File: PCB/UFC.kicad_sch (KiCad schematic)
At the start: 56 parts, among them M1 Fan_3pin, M2 Fan_3pin, M3 Fan_3pin, M4 Fan_3pin, M5 Fan_3pin, M6 Fan_3pin, M7 Fan_3pin, M8 Fan_3pin, SW1 PWM 12:5, U1 Pico

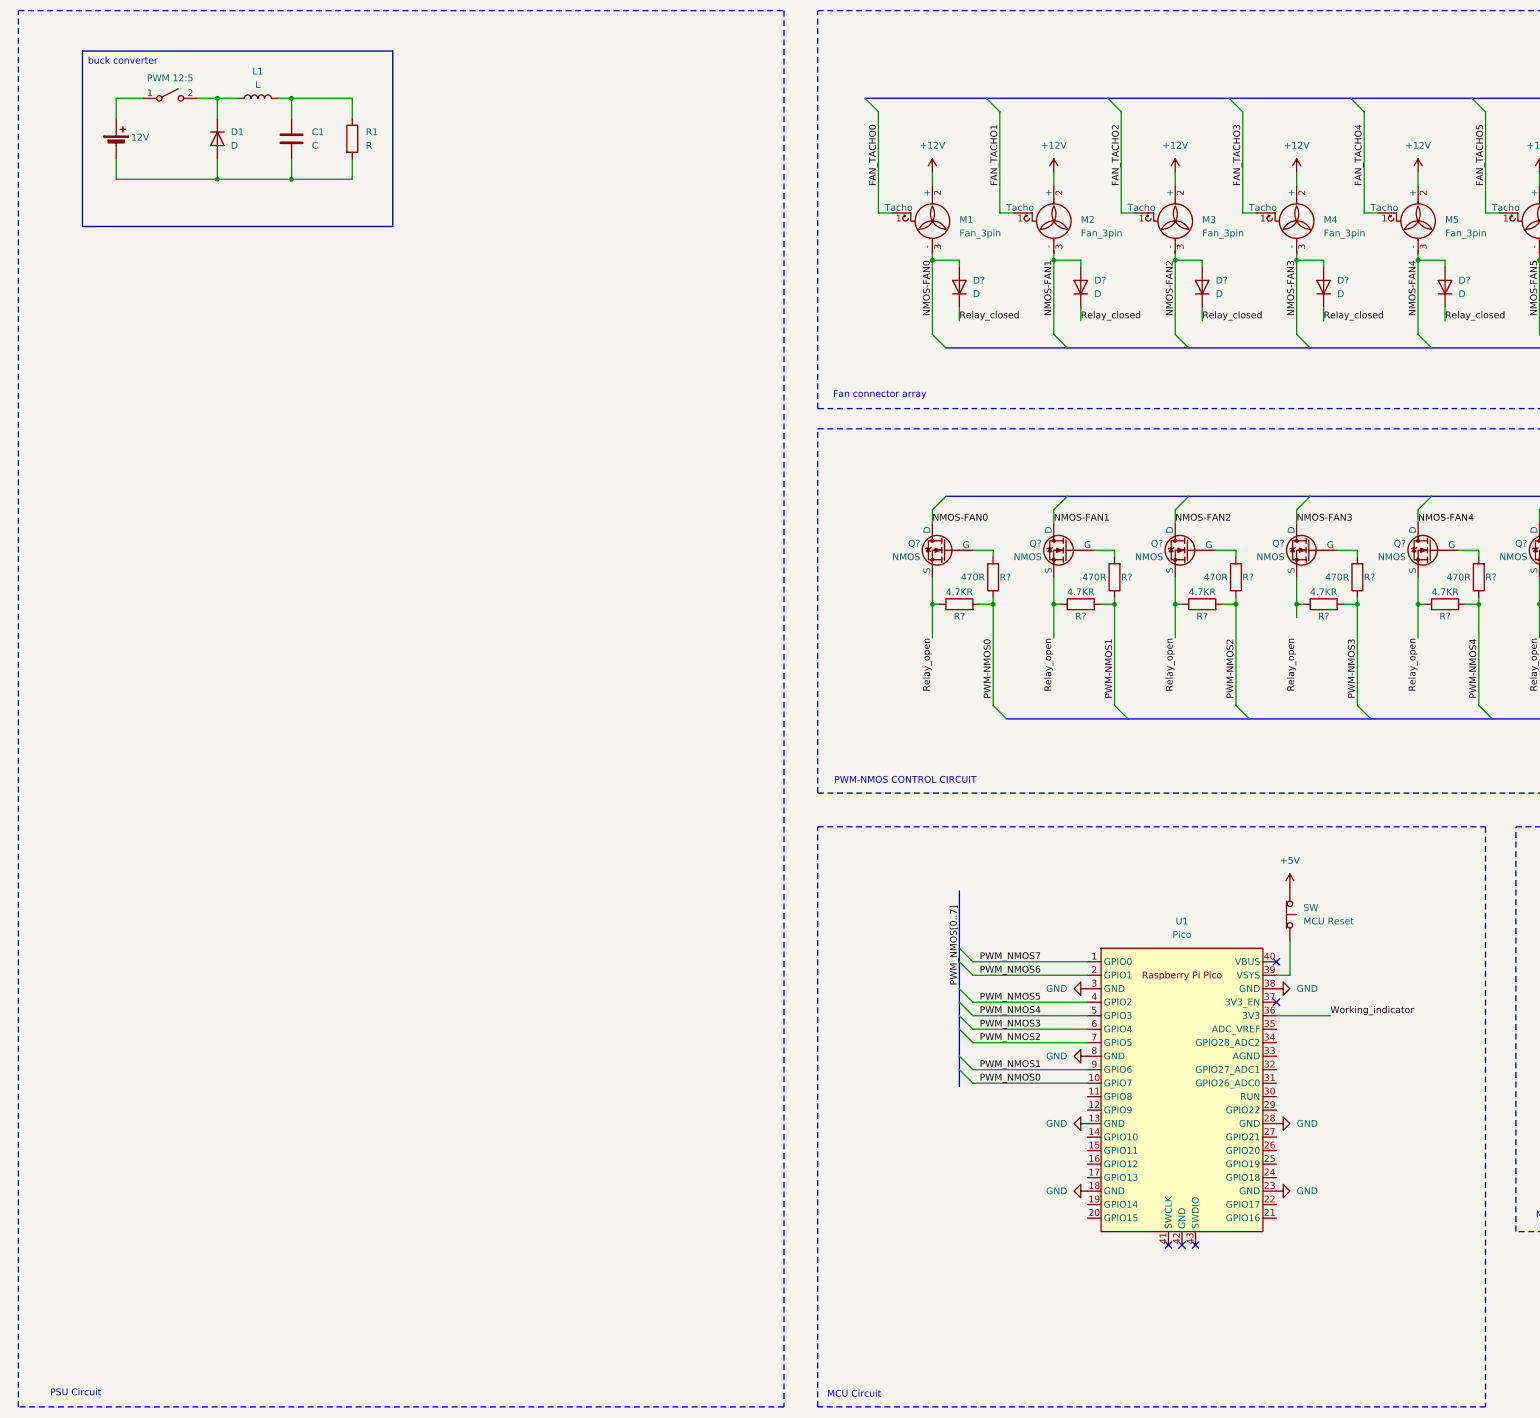
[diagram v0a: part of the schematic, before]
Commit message: Scheme circuit placement change
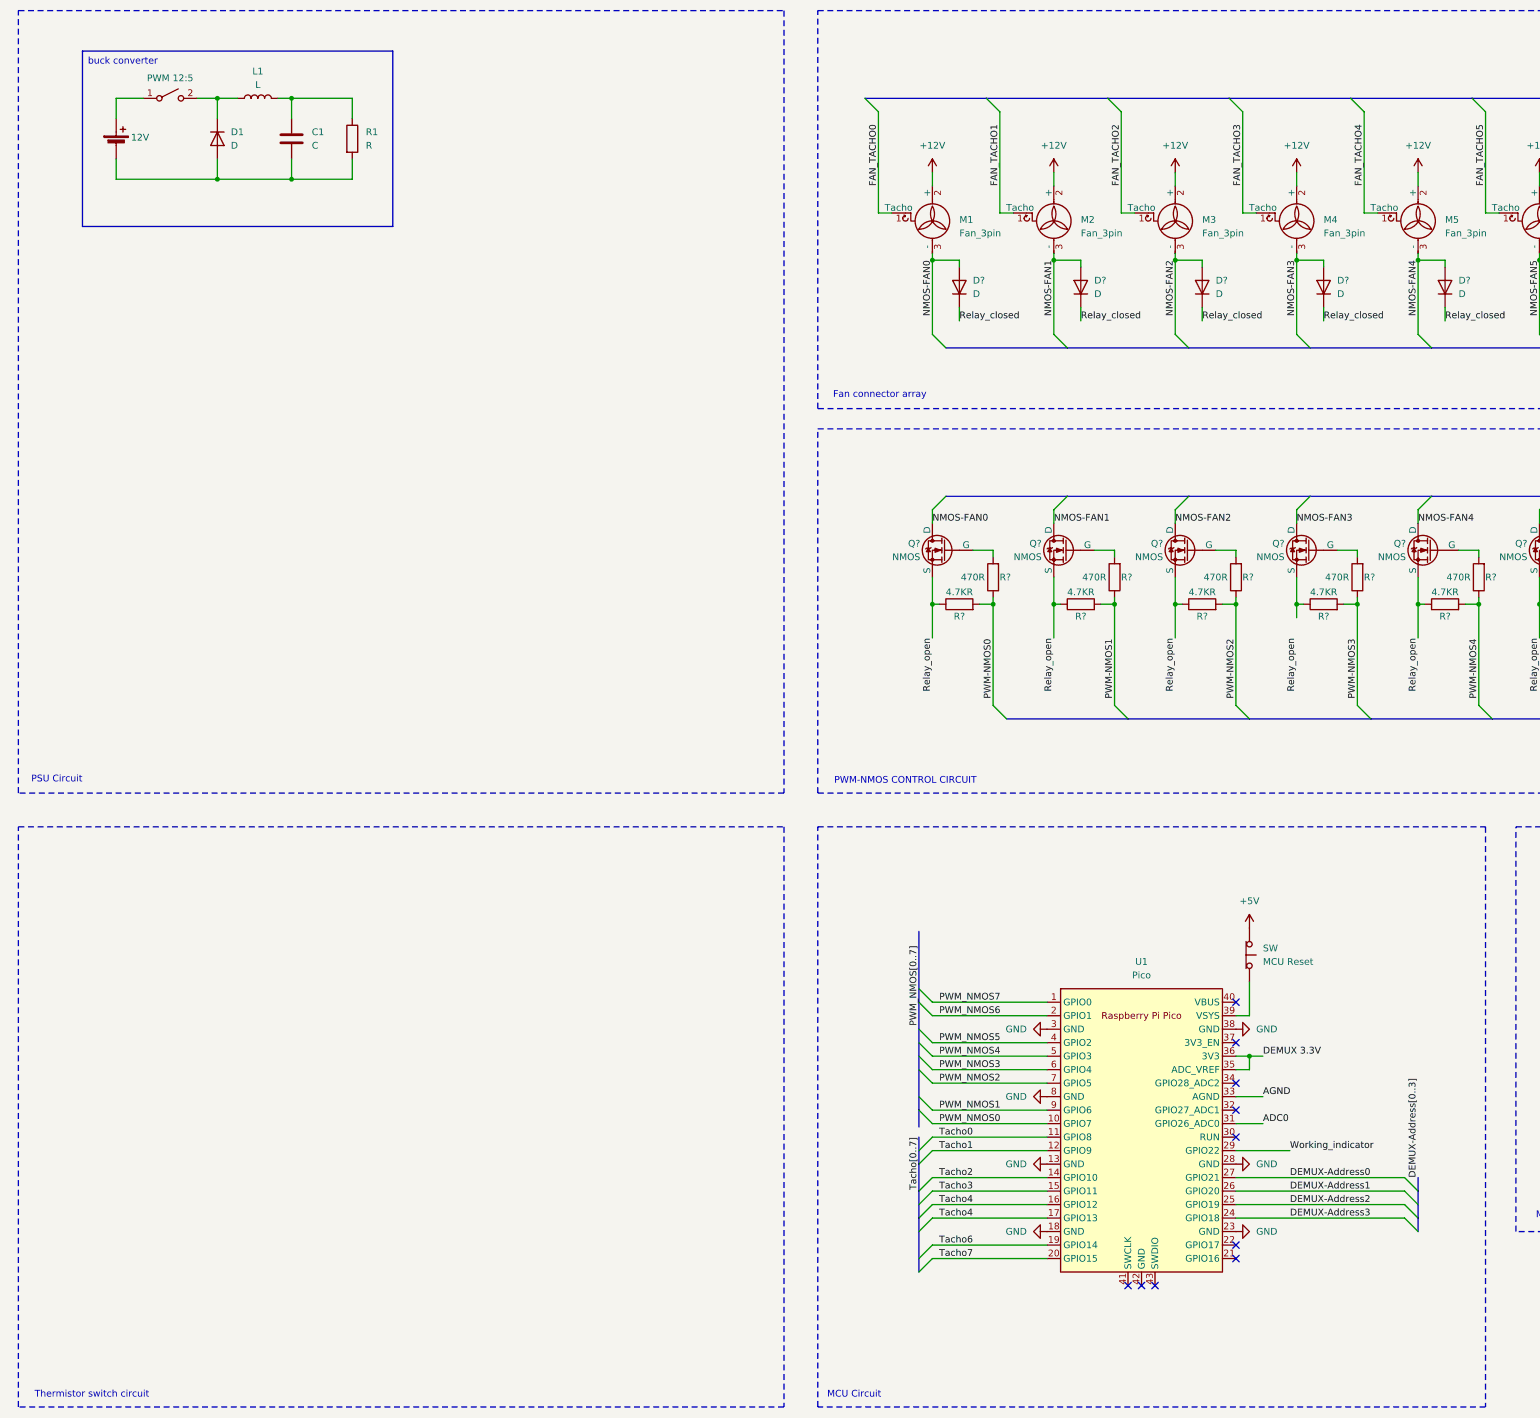
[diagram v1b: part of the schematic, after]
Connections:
- net Working_indicator: now also U1.29 (GPIO22); no longer U1.36 (3V3)
- net Tacho0: now reaches U1.11 (GPIO8)
- net Tacho1: now reaches U1.12 (GPIO9)
- net Tacho2: now reaches U1.14 (GPIO10)
- net Tacho3: now reaches U1.15 (GPIO11)
- net Tacho4: now reaches U1.16 (GPIO12)
- net Tacho4: now also U1.17 (GPIO13)
- net Tacho6: now reaches U1.19 (GPIO14)
- net Tacho7: now reaches U1.20 (GPIO15)
- net DEMUX-Address3: now reaches U1.24 (GPIO18)
- net DEMUX-Address2: now reaches U1.25 (GPIO19)
- net DEMUX-Address1: now reaches U1.26 (GPIO20)
- net DEMUX-Address0: now reaches U1.27 (GPIO21)
- net ADC0: now reaches U1.31 (GPIO26_ADC0)
- net AGND: now reaches U1.33 (AGND)
- net DEMUX 3.3V: now reaches U1.35 (ADC_VREF)
- net DEMUX 3.3V: now also U1.36 (3V3)
- no-connect marks 5 -> 10
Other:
- note added: "Thermistor switch circuit"
- moved on the sheet: SW, U1

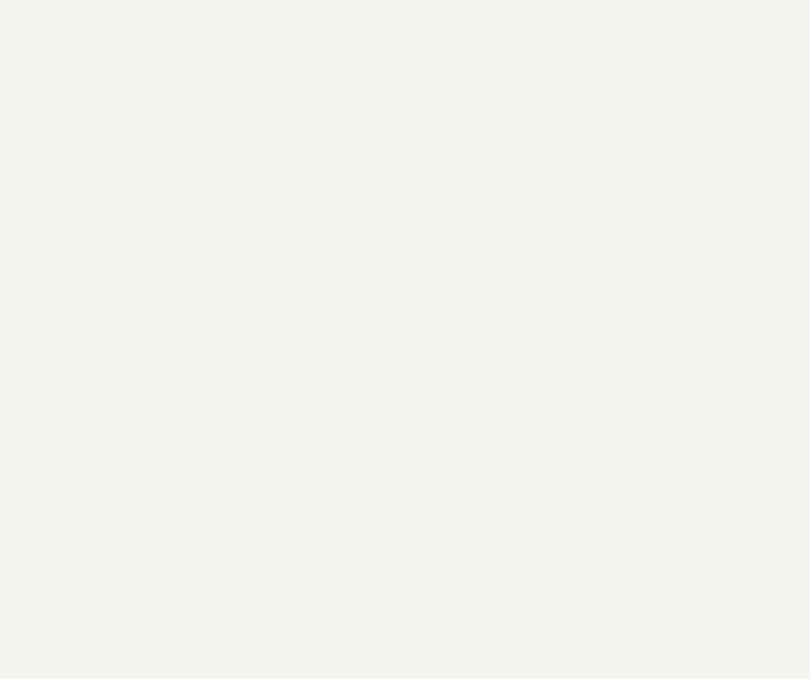
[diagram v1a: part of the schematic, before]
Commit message: Create symbol lib, add demux symbol
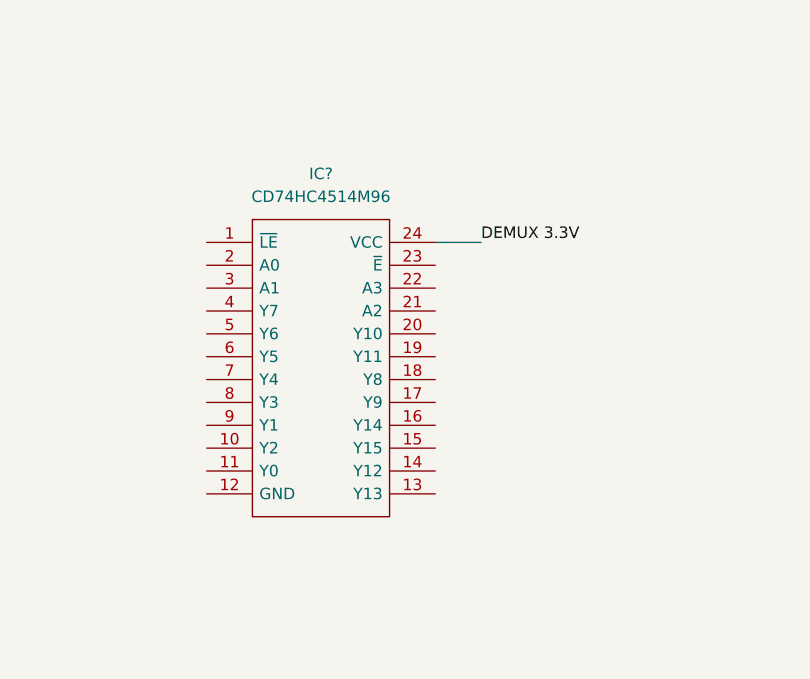
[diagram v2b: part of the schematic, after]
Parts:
- added IC?: CD74HC4514M96, SOIC127P1030X265-24N, symbol UFC_Lib:CD74HC4514M96
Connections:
- net DEMUX 3.3V: now also IC?.24 (VCC)
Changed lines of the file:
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@@
 	(wire
 		(pts
+			(xy 107.95 212.09) (xy 113.03 212.09)
+		)
+		(stroke
+			(width 0)
+			(type default)
+		)
+	)
+	(wire
+		(pts
 			(xy 259.08 64.77) (xy 259.08 78.74)
 		)
@@
 		)
 	)
+	(label "DEMUX 3.3V"
+		(at 113.03 212.09 0)
+		(fields_autoplaced yes)
+		(effects
+			(font
+				(size 1.27 1.27)
+			)
+			(justify left bottom)
+		)
+	)
 	(label "Relay_closed"
 		(at 264.16 76.2 0)
@@
 					(unit 1)
 				)
+			)
+		)
+	)
+	(symbol
+		(lib_id "UFC_Lib:CD74HC4514M96")
+		(at 82.55 212.09 0)
+		(unit 1)
+		(exclude_from_sim no)
+		(in_bom yes)
+		(on_board yes)
+		(dnp no)
+		(fields_autoplaced yes)
+		(property "Reference" "IC?"
+			(at 95.25 204.47 0)
+			(effects
+				(font
+					(size 1.27 1.27)
+				)
+			)
+		)
+		(property "Value" "CD74HC4514M96"
+			(at 95.25 207.01 0)
+			(effects
+				(font
+					(size 1.27 1.27)
+				)
+			)
+		)
+		(property "Footprint" "SOIC127P1030X265-24N"
+			(at 55.118 250.444 0)
+			(effects
+				(font
+					(size 1.27 1.27)
+				)
+				(justify left)
+				(hide yes)
+			)
+		)
+		(property "Datasheet" "http://www.ti.com/lit/gpn/cd74hc4514"
+			(at 55.118 252.984 0)
+			(effects
+				(font
+					(size 1.27 1.27)
+				)
+				(justify left)
+				(hide yes)
+			)
+		)
+		(property "Description" "High Speed CMOS Logic 4-to-16 Line Decoder/Demultiplexer with Input Latches"
+			(at 94.996 245.11 0)
+			(effects
+				(font
+					(size 1.27 1.27)
+				)
+				(hide yes)
+			)
+		)
+		(property "Description_1" "High Speed CMOS Logic 4-to-16 Line Decoder/Demultiplexer with Input Latches"
+			(at 55.118 255.524 0)
+			(effects
+				(font
+					(size 1.27 1.27)
+				)
+				(justify left)
+				(hide yes)
+			)
+		)
+		(property "Height" "2.65"
+			(at 76.454 247.904 0)
+			(effects
+				(font
+					(size 1.27 1.27)
+				)
+				(justify left)
+				(hide yes)
+			)
+		)
+		(property "Mouser Part Number" "595-CD74HC4514M96"
+			(at 55.118 260.604 0)
+			(effects
+				(font
+					(size 1.27 1.27)
+				)
+				(justify left)
+				(hide yes)
+			)
+		)
+		(property "Mouser Price/Stock" "https://www.mouser.co.uk/ProductDetail/Texas-Instruments/CD74HC4514M96?qs=xFfolx0DHx3s6ILXGQ%2FrLQ%3D%3D"
+			(at 55.118 263.144 0)
+			(effects
+				(font
+					(size 1.27 1.27)
+				)
+				(justify left)
+				(hide yes)
+			)
+		)
+		(property "Manufacturer_Name" "Texas Instruments"
+			(at 55.118 265.684 0)
+			(effects
+				(font
+					(size 1.27 1.27)
+				)
+				(justify left)
+				(hide yes)
+			)
+		)
+		(property "Manufacturer_Part_Number" "CD74HC4514M96"
+			(at 55.118 268.224 0)
+			(effects
+				(font
+					(size 1.27 1.27)
+				)
+				(justify left)
+				(hide yes)
+			)
+		)
+		(pin "12"
+		)
+		(pin "10"
+		)
+		(pin "14"
+		)
+		(pin "16"
+		)
+		(pin "17"
+		)
+		(pin "2"
+		)
+		(pin "8"
+		)
+		(pin "15"
+		)
+		(pin "3"
+		)
+		(pin "18"
+		)
+		(pin "7"
+		)
+		(pin "11"
+		)
+		(pin "20"
+		)
+		(pin "21"
+		)
+		(pin "22"
+		)
+		(pin "1"
+		)
+		(pin "23"
+		)
+		(pin "5"
+		)
+		(pin "6"
+		)
+		(pin "4"
+		)
+		(pin "13"
+		)
+		(pin "9"
+		)
+		(pin "19"
+		)
+		(pin "24"
+		)
+		(instances
+			(project ""
+				(path "/342a3fd1-b517-460b-a70f-feeb7547ac4b"
+					(reference "IC?")
+					(unit 1)
+				)

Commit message: Add thermistor switch prototype
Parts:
- added R?: 10KR, symbol Device:R
- added TH? (x3): Thermistor_NTC, symbol Device:Thermistor_NTC
- SW: value Emergency Switch -> Main Power Switch
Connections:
- net ADC0: now also R?.1, TH?.2, TH?.2, TH?.2
- net AGND: now also R?.2
- net DEMUX-Address0: now also IC?.2 (A0)
- net DEMUX-Address1: now also IC?.3 (A1)
- net DEMUX-Address2: now also IC?.21 (A2)
- net DEMUX-Address3: now also IC?.22 (A3)
- net GND: now also IC?.12 (GND)
- net at IC?.18 (Y8): now also TH?.1
- net at IC?.19 (Y11): now also TH?.1
- net at IC?.20 (Y10): now also TH?.1
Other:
- moved on the sheet: IC?
